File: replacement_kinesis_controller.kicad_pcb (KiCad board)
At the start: 2 copper layers, 99.1 x 86.4 mm, 104 parts, among them CN1 USB_general, CN2 Micro-USB, CN3 Mini-USB, CN4 USB_general, K1 CONN_3, K2 CONN_3, K3 CONN_3, K4 CONN_3, P1 CONN_3X2, P10 CONN_8, P11 CONN_5, P12 CONN_5, P13 CONN_6, P14 CONN_8, P15 CONN_5X2, P16 CONN_16, P17 CONN_16, P18 POWER, P19 PCM, P2 CONN_13, P20 UART, P21 SPI, P22 IO, P23 SMIRF, P25 USB, P3 CONN_13, P4 CONN_10, P5 CONN_10, P6 CONN_13, P7 CONN_13, P8 CONN_5X2, P9 CONN_6, SW3 SPST, SW4 SPST, U1 MCP23018-E, U2 WS2811_RGB_LED, U3 WS2811_RGB_LED, U4 WS2811_RGB_LED, U5 WS2811_RGB_LED, U9 MCP1700

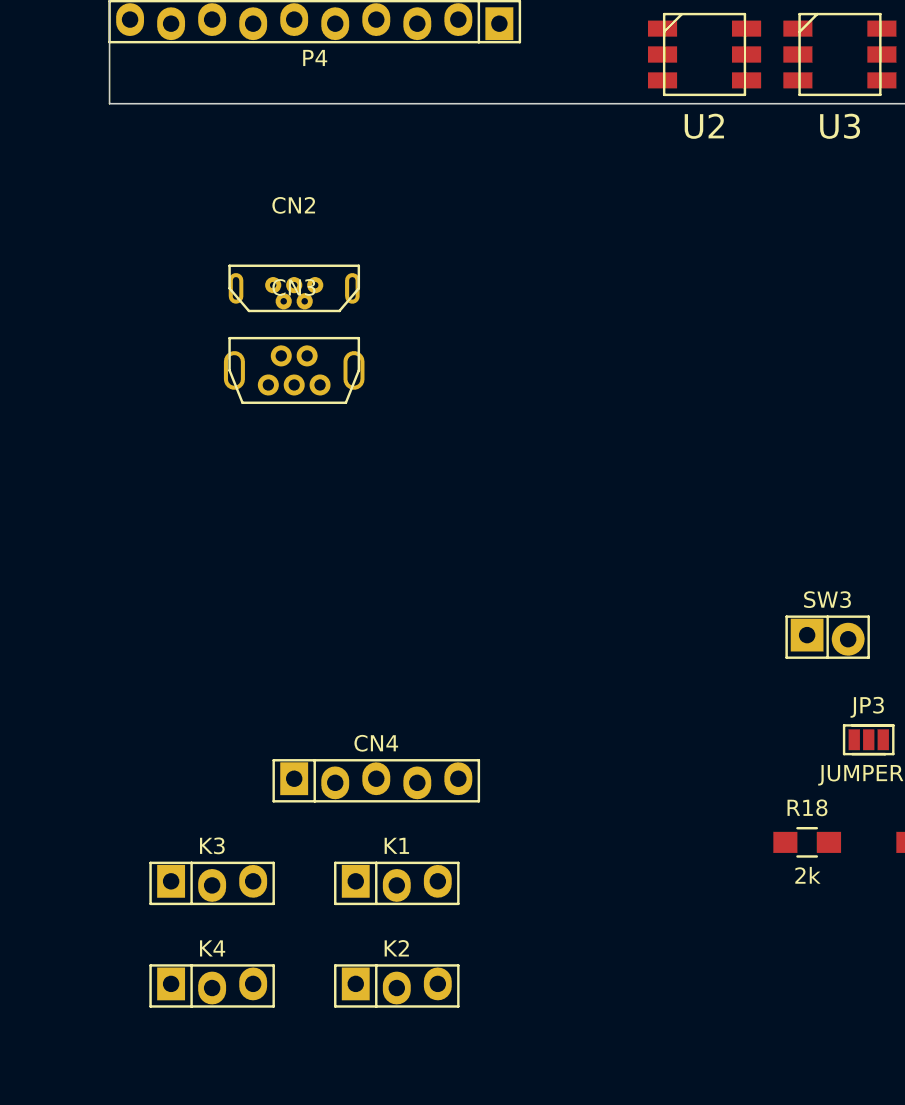
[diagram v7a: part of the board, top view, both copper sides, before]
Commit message: Add mockup of USB breakout
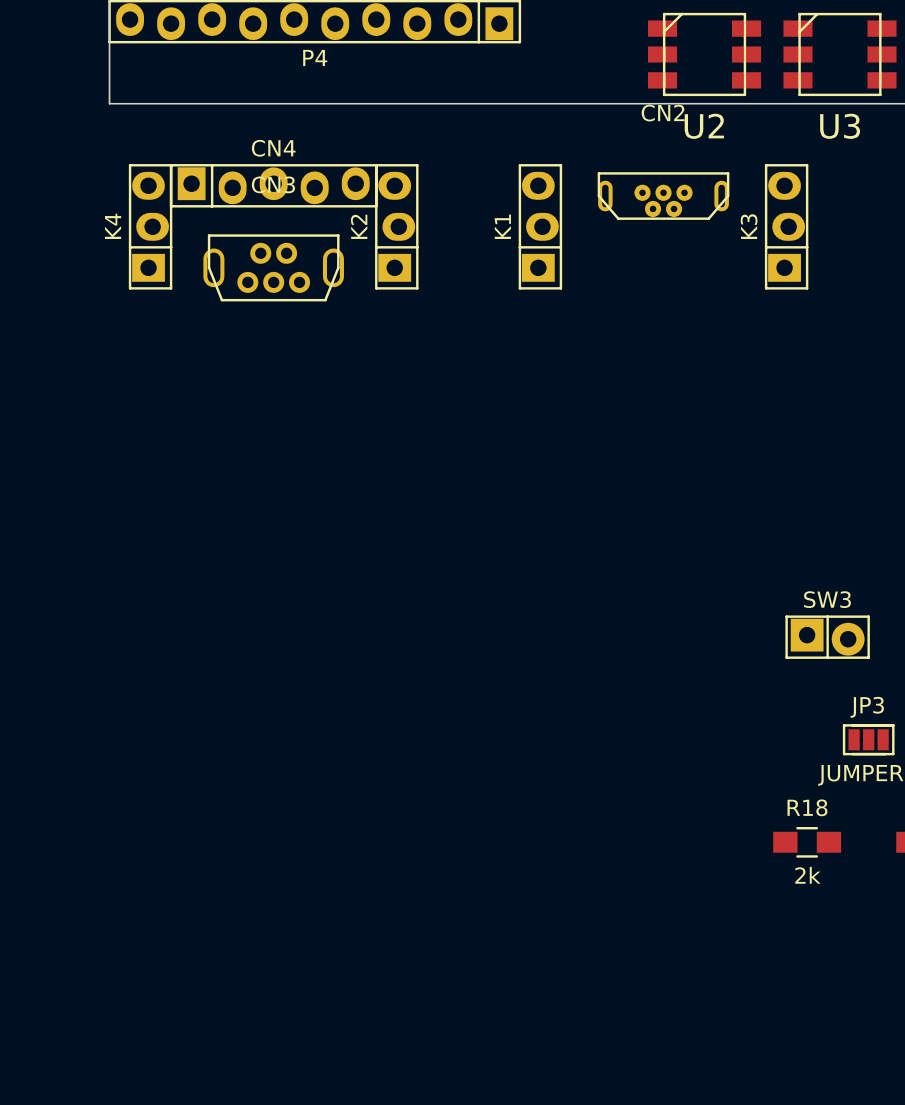
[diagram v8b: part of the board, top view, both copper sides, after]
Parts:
- moved K3 54.0 mm to (115.6, 137.2), turned to 90 degrees
- moved K4 47.1 mm to (76.2, 137.2), turned to 90 degrees
- moved K2 47.0 mm to (91.4, 137.2), turned to 90 degrees
- moved K1 41.6 mm to (100.3, 137.2), turned to 90 degrees
- moved CN4 37.4 mm to (83.8, 134.6)
- moved CN2 23.6 mm to (108.0, 135.3)
- moved CN3 6.48 mm to (83.8, 139.7)
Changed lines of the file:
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@@
     (links 292)
     (no_connects 292)
-    (area 73.609999 43.129999 172.770001 129.590001)
+    (area 23.412429 13.045 269.279001 199.979)
     (thickness 1.6)
-    (drawings 4)
+    (drawings 8)
     (tracks 0)
     (zones 0)
@@
   )
   (module replacement_kinesis_controller:Pin_Header_Staggered_Straight_1x05 (layer F.Cu)
-    (at 90.17 171.45)
+    (at 83.82 134.62)
     (descr "Through hole pin header")
     (tags "pin header")
@@
   )
   (module replacement_kinesis_controller:Pin_Header_Staggered_Straight_1x03 (layer F.Cu)
-    (at 91.44 177.8)
+    (at 100.33 137.16 90)
     (descr "Through hole pin header")
     (tags "pin header")
-    (fp_text reference K1 (at 0 -2.286) (layer F.SilkS)
+    (fp_text reference K1 (at 0 -2.286 90) (layer F.SilkS)
       (effects (font (size 1 1) (thickness 0.15)))
     )
-    (fp_text value CONN_3 (at 0 0) (layer F.SilkS) hide
+    (fp_text value CONN_3 (at 0 0 90) (layer F.SilkS) hide
       (effects (font (size 1 1) (thickness 0.15)))
     )
@@
     (fp_line (start -3.81 -1.27) (end -3.81 1.27) (layer F.SilkS) (width 0.15))
     (fp_line (start -3.81 1.27) (end -1.27 1.27) (layer F.SilkS) (width 0.15))
-    (pad 1 thru_hole rect (at -2.54 -0.127) (size 1.7272 2.032) (drill 1.016) (layers *.Cu *.Mask F.SilkS)
+    (pad 1 thru_hole rect (at -2.54 -0.127 90) (size 1.7272 2.032) (drill 1.016) (layers *.Cu *.Mask F.SilkS)
       (net 16 "Net-(CN2-Pad~)"))
-    (pad 2 thru_hole oval (at 0 0.127) (size 1.7272 2.032) (drill 1.016) (layers *.Cu *.Mask F.SilkS)
+    (pad 2 thru_hole oval (at 0 0.127 90) (size 1.7272 2.032) (drill 1.016) (layers *.Cu *.Mask F.SilkS)
       (net 16 "Net-(CN2-Pad~)"))
-    (pad 3 thru_hole oval (at 2.54 -0.127) (size 1.7272 2.032) (drill 1.016) (layers *.Cu *.Mask F.SilkS)
+    (pad 3 thru_hole oval (at 2.54 -0.127 90) (size 1.7272 2.032) (drill 1.016) (layers *.Cu *.Mask F.SilkS)
       (net 16 "Net-(CN2-Pad~)"))
     (model Pin_Headers/Pin_Header_Straight_1x03.wrl
@@
   )
   (module replacement_kinesis_controller:Pin_Header_Staggered_Straight_1x03 (layer F.Cu)
-    (at 91.44 184.15)
+    (at 91.44 137.16 90)
     (descr "Through hole pin header")
     (tags "pin header")
-    (fp_text reference K2 (at 0 -2.286) (layer F.SilkS)
+    (fp_text reference K2 (at 0 -2.286 90) (layer F.SilkS)
       (effects (font (size 1 1) (thickness 0.15)))
     )
-    (fp_text value CONN_3 (at 0 0) (layer F.SilkS) hide
+    (fp_text value CONN_3 (at 0 0 90) (layer F.SilkS) hide
       (effects (font (size 1 1) (thickness 0.15)))
     )
@@
     (fp_line (start -3.81 -1.27) (end -3.81 1.27) (layer F.SilkS) (width 0.15))
     (fp_line (start -3.81 1.27) (end -1.27 1.27) (layer F.SilkS) (width 0.15))
-    (pad 1 thru_hole rect (at -2.54 -0.127) (size 1.7272 2.032) (drill 1.016) (layers *.Cu *.Mask F.SilkS)
+    (pad 1 thru_hole rect (at -2.54 -0.127 90) (size 1.7272 2.032) (drill 1.016) (layers *.Cu *.Mask F.SilkS)
       (net 17 "Net-(CN3-Pad~)"))
-    (pad 2 thru_hole oval (at 0 0.127) (size 1.7272 2.032) (drill 1.016) (layers *.Cu *.Mask F.SilkS)
+    (pad 2 thru_hole oval (at 0 0.127 90) (size 1.7272 2.032) (drill 1.016) (layers *.Cu *.Mask F.SilkS)
       (net 17 "Net-(CN3-Pad~)"))
-    (pad 3 thru_hole oval (at 2.54 -0.127) (size 1.7272 2.032) (drill 1.016) (layers *.Cu *.Mask F.SilkS)
+    (pad 3 thru_hole oval (at 2.54 -0.127 90) (size 1.7272 2.032) (drill 1.016) (layers *.Cu *.Mask F.SilkS)
       (net 17 "Net-(CN3-Pad~)"))
     (model Pin_Headers/Pin_Header_Straight_1x03.wrl
@@
   )
   (module replacement_kinesis_controller:Pin_Header_Staggered_Straight_1x03 (layer F.Cu)
-    (at 80.01 177.8)
+    (at 115.57 137.16 90)
     (descr "Through hole pin header")
     (tags "pin header")
-    (fp_text reference K3 (at 0 -2.286) (layer F.SilkS)
+    (fp_text reference K3 (at 0 -2.286 90) (layer F.SilkS)
       (effects (font (size 1 1) (thickness 0.15)))
     )
-    (fp_text value CONN_3 (at 0 0) (layer F.SilkS) hide
+    (fp_text value CONN_3 (at 0 0 90) (layer F.SilkS) hide
       (effects (font (size 1 1) (thickness 0.15)))
     )
@@
     (fp_line (start -3.81 -1.27) (end -3.81 1.27) (layer F.SilkS) (width 0.15))
     (fp_line (start -3.81 1.27) (end -1.27 1.27) (layer F.SilkS) (width 0.15))
-    (pad 1 thru_hole rect (at -2.54 -0.127) (size 1.7272 2.032) (drill 1.016) (layers *.Cu *.Mask F.SilkS)
+    (pad 1 thru_hole rect (at -2.54 -0.127 90) (size 1.7272 2.032) (drill 1.016) (layers *.Cu *.Mask F.SilkS)
       (net 16 "Net-(CN2-Pad~)"))
-    (pad 2 thru_hole oval (at 0 0.127) (size 1.7272 2.032) (drill 1.016) (layers *.Cu *.Mask F.SilkS)
+    (pad 2 thru_hole oval (at 0 0.127 90) (size 1.7272 2.032) (drill 1.016) (layers *.Cu *.Mask F.SilkS)
       (net 16 "Net-(CN2-Pad~)"))
-    (pad 3 thru_hole oval (at 2.54 -0.127) (size 1.7272 2.032) (drill 1.016) (layers *.Cu *.Mask F.SilkS)
+    (pad 3 thru_hole oval (at 2.54 -0.127 90) (size 1.7272 2.032) (drill 1.016) (layers *.Cu *.Mask F.SilkS)
       (net 16 "Net-(CN2-Pad~)"))
     (model Pin_Headers/Pin_Header_Straight_1x03.wrl
@@
   )
   (module replacement_kinesis_controller:Pin_Header_Staggered_Straight_1x03 (layer F.Cu)
-    (at 80.01 184.15)
+    (at 76.2 137.16 90)
     (descr "Through hole pin header")
     (tags "pin header")
-    (fp_text reference K4 (at 0 -2.286) (layer F.SilkS)
+    (fp_text reference K4 (at 0 -2.286 90) (layer F.SilkS)
       (effects (font (size 1 1) (thickness 0.15)))
     )
-    (fp_text value CONN_3 (at 0 0) (layer F.SilkS) hide
+    (fp_text value CONN_3 (at 0 0 90) (layer F.SilkS) hide
       (effects (font (size 1 1) (thickness 0.15)))
     )
@@
     (fp_line (start -3.81 -1.27) (end -3.81 1.27) (layer F.SilkS) (width 0.15))
     (fp_line (start -3.81 1.27) (end -1.27 1.27) (layer F.SilkS) (width 0.15))
-    (pad 1 thru_hole rect (at -2.54 -0.127) (size 1.7272 2.032) (drill 1.016) (layers *.Cu *.Mask F.SilkS)
+    (pad 1 thru_hole rect (at -2.54 -0.127 90) (size 1.7272 2.032) (drill 1.016) (layers *.Cu *.Mask F.SilkS)
       (net 17 "Net-(CN3-Pad~)"))
-    (pad 2 thru_hole oval (at 0 0.127) (size 1.7272 2.032) (drill 1.016) (layers *.Cu *.Mask F.SilkS)
+    (pad 2 thru_hole oval (at 0 0.127 90) (size 1.7272 2.032) (drill 1.016) (layers *.Cu *.Mask F.SilkS)
       (net 17 "Net-(CN3-Pad~)"))
-    (pad 3 thru_hole oval (at 2.54 -0.127) (size 1.7272 2.032) (drill 1.016) (layers *.Cu *.Mask F.SilkS)
+    (pad 3 thru_hole oval (at 2.54 -0.127 90) (size 1.7272 2.032) (drill 1.016) (layers *.Cu *.Mask F.SilkS)
       (net 17 "Net-(CN3-Pad~)"))
     (model Pin_Headers/Pin_Header_Straight_1x03.wrl
@@
   )
   (module replacement_kinesis_controller:USB_micro_B-vertical (layer F.Cu)
-    (at 85.09 140.97)
+    (at 107.95 135.255)
     (descr "Through hole pin header")
     (tags "pin header")
@@
   )
   (module replacement_kinesis_controller:USB_mini_B-vertical (layer F.Cu)
-    (at 85.09 146.05)
+    (at 83.82 139.7)
     (descr "Through hole pin header")
     (tags "pin header")
@@
     )
   )
+  (gr_line (start 172.72 142.24) (end 171.45 142.24) (angle 90) (layer F.Fab) (width 0.2))
+  (gr_line (start 172.72 140.97) (end 172.72 142.24) (angle 90) (layer F.Fab) (width 0.2))
+  (gr_line (start 73.66 142.24) (end 74.93 142.24) (angle 90) (layer F.Fab) (width 0.2))
+  (gr_line (start 73.66 140.97) (end 73.66 142.24) (angle 90) (layer F.Fab) (width 0.2))
   (gr_line (start 73.66 129.54) (end 73.66 43.18) (angle 90) (layer Edge.Cuts) (width 0.1))
   (gr_line (start 172.72 129.54) (end 73.66 129.54) (angle 90) (layer Edge.Cuts) (width 0.1))
